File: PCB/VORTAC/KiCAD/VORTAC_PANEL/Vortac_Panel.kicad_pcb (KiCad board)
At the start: 4 copper layers, 80 x 80 mm, 103 parts, among them IC1 TMC2209-LA, J1 Conn_02x02_Odd_Even, J1 DEBUG, J14 918-418K2023S40001, J15 STEPPER, J2 Conn_02x03_Odd_Even, J3 Conn_01x07, J3 Conn_02x02_Odd_Even, SW1 Boot, SW2 Reset, U1 TLV73333PDBV, U2 STM32F103C8T6, U3 EE-SX4320, U5 AS5047D, U6 AP63205WU, U7 EE-SX3350, U8 TJA1044GTK/3Z, X1 Logo Gold, Y1 8MHz

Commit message: Panel Progress
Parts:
- removed the mouse-bite-2mm-slot at (98.8, 49.0)
- removed the mouse-bite-2mm-slot at (121.0, 73.0)
- added D1: SP0502BAHT, Package_TO_SOT_SMD:SOT-23, B.Cu at (91.5, 90.8)
- added D1: SP0502BAHT, Package_TO_SOT_SMD:SOT-23, B.Cu at (104.1, 105.5)
- added D1: SP0502BAHT, Package_TO_SOT_SMD:SOT-23, B.Cu at (91.6, 108.2)
- added D1: SP0502BAHT, Package_TO_SOT_SMD:SOT-23, B.Cu at (138.6, 108.2)
- added D2: SP0502BAHT, Package_TO_SOT_SMD:SOT-23, B.Cu at (81.8, 90.8)
- added D2: SP0502BAHT, Package_TO_SOT_SMD:SOT-23, B.Cu at (128.8, 108.2)
- added D2: SP0502BAHT, Package_TO_SOT_SMD:SOT-23, B.Cu at (81.8, 108.2)
- added D2: SP0502BAHT, Package_TO_SOT_SMD:SOT-23, B.Cu at (113.8, 105.6)
- added H1: MountingHole_Pad, Vortac:MountingHole_2.2mm_M2_Pad_Via_NTR, B.Cu at (77.6, 84.6)
- added H1: MountingHole_Pad, Vortac:MountingHole_2.2mm_M2_Pad_Via_NTR, B.Cu at (118.0, 111.7)
- added H1: MountingHole_Pad, Vortac:MountingHole_2.2mm_M2_Pad_Via_NTR, B.Cu at (77.6, 102.0)
- added H1: MountingHole_Pad, Vortac:MountingHole_2.2mm_M2_Pad_Via_NTR, B.Cu at (124.6, 102.0)
- added H2: MountingHole_Pad, Vortac:MountingHole_2.2mm_M2_Pad_Via_NTR, B.Cu at (143.0, 109.6)
- added H2: MountingHole_Pad, Vortac:MountingHole_2.2mm_M2_Pad_Via_NTR, B.Cu at (96.0, 109.6)
- added H2: MountingHole_Pad, Vortac:MountingHole_2.2mm_M2_Pad_Via_NTR, B.Cu at (99.7, 104.2)
- added H2: MountingHole_Pad, Vortac:MountingHole_2.2mm_M2_Pad_Via_NTR, B.Cu at (96.0, 92.2)
- added J1: Conn_01x07, Vortac:mill-max-0881-1-15-20-82-14-11-0_LandingPads_ContactPad_PTH_2x1.5x1, B.Cu at (127.6, 104.8)
- added J1: Conn_01x07, Vortac:mill-max-0881-1-15-20-82-14-11-0_LandingPads_ContactPad_PTH_2x1.5x1, B.Cu at (80.5, 87.4)
- added J1: Conn_01x07, Vortac:mill-max-0881-1-15-20-82-14-11-0_LandingPads_ContactPad_PTH_2x1.5x1, B.Cu at (115.1, 109.0)
- added J1: Conn_01x07, Vortac:mill-max-0881-1-15-20-82-14-11-0_LandingPads_ContactPad_PTH_2x1.5x1, B.Cu at (80.6, 104.8)
- added J2: Conn_01x02, Vortac:Toolplate_Solderpoint_01x02_Power, B.Cu at (123.9, 112.2)
- added J2: Conn_01x02, Vortac:Toolplate_Solderpoint_01x02_Power, B.Cu at (118.7, 101.5)
- added J2: Conn_01x02, Vortac:Toolplate_Solderpoint_01x02_Power, B.Cu at (76.9, 112.2)
- added J2: Conn_01x02, Vortac:Toolplate_Solderpoint_01x02_Power, B.Cu at (76.9, 94.8)
- added J3: Conn_01x05, Vortac:Toolplate_Solderpoint_01x05_Data, B.Cu at (83.8, 112.9)
- added J3: Conn_01x05, Vortac:Toolplate_Solderpoint_01x05_Data, B.Cu at (83.8, 95.5)
- added J3: Conn_01x05, Vortac:Toolplate_Solderpoint_01x05_Data, B.Cu at (130.8, 112.9)
- added J3: Conn_01x05, Vortac:Toolplate_Solderpoint_01x05_Data, B.Cu at (111.8, 100.8)
- added mouse-bite-2mm-slot: VAL**, Vortac:mouse-bite-2mm-slot, F.Cu at (130.4, 98.2)
- added mouse-bite-2mm-slot: VAL**, Vortac:mouse-bite-2mm-slot, F.Cu at (85.0, 98.2)
- added mouse-bite-2mm-slot: VAL**, Vortac:mouse-bite-2mm-slot, F.Cu at (130.9, 115.6)
- added mouse-bite-2mm-slot: VAL**, Vortac:mouse-bite-2mm-slot, F.Cu at (131.8, 92.0)
- added mouse-bite-2mm-slot: VAL**, Vortac:mouse-bite-2mm-slot, F.Cu at (110.1, 115.6)
- added mouse-bite-2mm-slot: VAL**, Vortac:mouse-bite-2mm-slot, F.Cu at (110.4, 84.4)
- added mouse-bite-2mm-slot: VAL**, Vortac:mouse-bite-2mm-slot, F.Cu at (121.0, 72.9)
- added mouse-bite-2mm-slot: VAL**, Vortac:mouse-bite-2mm-slot, F.Cu at (81.0, 115.6)
- added mouse-bite-2mm-slot: VAL**, Vortac:mouse-bite-2mm-slot, F.Cu at (145.9, 93.5)
- added mouse-bite-2mm-slot: VAL**, Vortac:mouse-bite-2mm-slot, F.Cu at (96.3, 49.0)
- added mouse-bite-2mm-slot: VAL**, Vortac:mouse-bite-2mm-slot, F.Cu at (85.8, 80.8)
- added mouse-bite-2mm-slot: VAL**, Vortac:mouse-bite-2mm-slot, F.Cu at (109.6, 98.2)
- added mouse-bite-2mm-slot: VAL**, Vortac:mouse-bite-2mm-slot, F.Cu at (90.0, 115.6)
- added mouse-bite-2mm-slot: VAL**, Vortac:mouse-bite-2mm-slot, F.Cu at (95.3, 84.8)
- moved ? 10.8 mm to (141.2, 119.6) (x2)
- moved ? 10.8 mm to (141.2, 45.0) (x2)
- moved REF** 9.83 mm to (146.2, 119.6)
- moved ? 9.81 mm to (146.2, 45.0)
- moved REF** 2.24 mm to (79.8, 119.6)
- moved ? 2.17 mm to (79.8, 45.0)
- moved ? 1.30 mm to (84.8, 119.6)
- moved REF** 1.30 mm to (84.8, 119.6)
- moved ? 1.17 mm to (84.8, 45.0) (x2)
- moved mouse-bite-2mm-slot 0.40 mm to (128.7, 49.0)
- moved mouse-bite-2mm-slot 0.30 mm to (144.4, 73.1)
- moved mouse-bite-2mm-slot 0.30 mm to (136.8, 73.1)
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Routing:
- net USB_90_D-: track 0.00 -> 52.0 mm
- net TOOL_ID: track 0.00 -> 46.7 mm
- net CAN_H: track 62.4 -> 107.8 mm
- net USB_90_D+: track 0.00 -> 39.2 mm
- net CAN_L: track 58.2 -> 96.2 mm
- added copper zone on F.Cu, net VDC
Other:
- board size 80 x 80 mm -> 76.4 x 80.6 mm
- board text added: "25.05.25"
- board text added: "VORTAC REV01"
- board text added: "by Joel & Henny"

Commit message: updated Outlines
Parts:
- removed the D1 at (91.5, 90.8)
- removed the D1 at (104.1, 105.5)
- removed the D1 at (91.6, 108.2)
- removed the D1 at (138.6, 108.2)
- removed the D2 at (81.8, 90.8)
- removed the D2 at (128.8, 108.2)
- removed the D2 at (81.8, 108.2)
- removed the D2 at (113.8, 105.6)
- removed the H1 at (77.6, 84.6)
- removed the H1 at (118.0, 111.7)
- removed the H1 at (77.6, 102.0)
- removed the H1 at (124.6, 102.0)
- removed the H2 at (143.0, 109.6)
- removed the H2 at (96.0, 109.6)
- removed the H2 at (99.7, 104.2)
- removed the H2 at (96.0, 92.2)
- removed the J1 at (127.6, 104.8)
- removed the J1 at (80.5, 87.4)
- removed the J1 at (115.1, 109.0)
- removed the J1 at (80.6, 104.8)
- removed the J2 at (123.9, 112.2)
- removed the J2 at (118.7, 101.5)
- removed the J2 at (76.9, 112.2)
- removed the J2 at (76.9, 94.8)
- removed the J3 at (83.8, 112.9)
- removed the J3 at (83.8, 95.5)
- removed the J3 at (130.8, 112.9)
- removed the J3 at (111.8, 100.8)
- removed the mouse-bite-2mm-slot at (130.4, 98.2)
- removed the mouse-bite-2mm-slot at (85.0, 98.2)
- removed the mouse-bite-2mm-slot at (130.9, 115.6)
- removed the mouse-bite-2mm-slot at (110.1, 115.6)
- removed the mouse-bite-2mm-slot at (110.4, 84.4)
- removed the mouse-bite-2mm-slot at (81.0, 115.6)
- removed the mouse-bite-2mm-slot at (85.8, 80.8)
- removed the mouse-bite-2mm-slot at (109.6, 98.2)
- removed the mouse-bite-2mm-slot at (90.0, 115.6)
- removed the mouse-bite-2mm-slot at (95.3, 84.8)
- added D1: UDD32C24L01, Diode_SMD:D_SOD-323, F.Cu at (135.3, 103.5)
- added D1: UDD32C24L01, Diode_SMD:D_SOD-323, F.Cu at (86.9, 103.5)
- added D1: UDD32C24L01, Diode_SMD:D_SOD-323, F.Cu at (102.4, 110.3)
- added D1: UDD32C24L01, Diode_SMD:D_SOD-323, F.Cu at (86.9, 86.1)
- added D2: UDD32C24L01, Diode_SMD:D_SOD-323, F.Cu at (137.2, 103.5)
- added D2: UDD32C24L01, Diode_SMD:D_SOD-323, F.Cu at (100.5, 110.3)
- added D2: UDD32C24L01, Diode_SMD:D_SOD-323, F.Cu at (88.8, 103.5)
- added D2: UDD32C24L01, Diode_SMD:D_SOD-323, F.Cu at (88.8, 86.1)
- added D3: SD05, Diode_SMD:D_SOD-323, F.Cu at (106.8, 110.3)
- added D3: SD05, Diode_SMD:D_SOD-323, F.Cu at (82.5, 103.5)
- added D3: SD05, Diode_SMD:D_SOD-323, F.Cu at (131.0, 103.5)
- added D3: SD05, Diode_SMD:D_SOD-323, F.Cu at (82.5, 86.1)
- added D4: SD05, Diode_SMD:D_SOD-323, F.Cu at (104.9, 110.3)
- added D4: SD05, Diode_SMD:D_SOD-323, F.Cu at (84.4, 103.5)
- added D4: SD05, Diode_SMD:D_SOD-323, F.Cu at (132.9, 103.5)
- added D4: SD05, Diode_SMD:D_SOD-323, F.Cu at (84.4, 86.1)
- added D9: PTVS26VS1UR,115-ES, Diode_SMD:D_SOD-123F, F.Cu at (78.5, 87.2)
- added D9: PTVS26VS1UR,115-ES, Diode_SMD:D_SOD-123F, F.Cu at (110.8, 109.1)
- added D9: PTVS26VS1UR,115-ES, Diode_SMD:D_SOD-123F, F.Cu at (126.9, 104.6)
- added D9: PTVS26VS1UR,115-ES, Diode_SMD:D_SOD-123F, F.Cu at (78.5, 104.6)
- added H1: MountingHole_Pad, Vortac:MountingHole_2.2mm_M2_Pad_Via_NTR, F.Cu at (74.0, 111.7)
- added H1: MountingHole_Pad, Vortac:MountingHole_2.2mm_M2_Pad_Via_NTR, F.Cu at (115.3, 102.0)
- added H1: MountingHole_Pad, Vortac:MountingHole_2.2mm_M2_Pad_Via_NTR, F.Cu at (74.0, 94.3)
- added H1: MountingHole_Pad, Vortac:MountingHole_2.2mm_M2_Pad_Via_NTR, F.Cu at (122.4, 111.7)
- added H2: MountingHole_Pad, Vortac:MountingHole_2.2mm_M2_Pad_Via_NTR, F.Cu at (140.8, 104.2)
- added H2: MountingHole_Pad, Vortac:MountingHole_2.2mm_M2_Pad_Via_NTR, F.Cu at (92.3, 86.8)
- added H2: MountingHole_Pad, Vortac:MountingHole_2.2mm_M2_Pad_Via_NTR, F.Cu at (97.0, 109.6)
- added H2: MountingHole_Pad, Vortac:MountingHole_2.2mm_M2_Pad_Via_NTR, F.Cu at (92.3, 104.2)
- added J1: Conn_01x07, Vortac:mill-max-0881-1-15-20-82-14-11-0_LandingPads_ContactPad_PTH_2x1.5x1, F.Cu at (76.9, 109.0)
- added J1: Conn_01x07, Vortac:mill-max-0881-1-15-20-82-14-11-0_LandingPads_ContactPad_PTH_2x1.5x1, F.Cu at (76.9, 91.6)
- added J1: Conn_01x07, Vortac:mill-max-0881-1-15-20-82-14-11-0_LandingPads_ContactPad_PTH_2x1.5x1, F.Cu at (112.4, 104.8)
- added J1: Conn_01x07, Vortac:mill-max-0881-1-15-20-82-14-11-0_LandingPads_ContactPad_PTH_2x1.5x1, F.Cu at (125.4, 109.0)
- added J2: Conn_01x02, Vortac:Toolplate_Solderpoint_01x02_Power, F.Cu at (73.3, 84.1)
- added J2: Conn_01x02, Vortac:Toolplate_Solderpoint_01x02_Power, F.Cu at (121.7, 101.5)
- added J2: Conn_01x02, Vortac:Toolplate_Solderpoint_01x02_Power, F.Cu at (73.3, 101.5)
- added J2: Conn_01x02, Vortac:Toolplate_Solderpoint_01x02_Power, F.Cu at (116.0, 112.2)
- added J3: Conn_01x05, Vortac:Toolplate_Solderpoint_01x05_Data, F.Cu at (80.2, 100.8)
- added J3: Conn_01x05, Vortac:Toolplate_Solderpoint_01x05_Data, F.Cu at (128.6, 100.8)
- added J3: Conn_01x05, Vortac:Toolplate_Solderpoint_01x05_Data, F.Cu at (109.2, 112.9)
- added J3: Conn_01x05, Vortac:Toolplate_Solderpoint_01x05_Data, F.Cu at (80.2, 83.4)
- added mouse-bite-2mm-slot: VAL**, Vortac:mouse-bite-2mm-slot, F.Cu at (105.4, 98.2)
- added mouse-bite-2mm-slot: VAL**, Vortac:mouse-bite-2mm-slot, F.Cu at (81.4, 115.6)
- added mouse-bite-2mm-slot: VAL**, Vortac:mouse-bite-2mm-slot, F.Cu at (128.2, 98.2)
- added mouse-bite-2mm-slot: VAL**, Vortac:mouse-bite-2mm-slot, F.Cu at (74.9, 80.8)
- added mouse-bite-2mm-slot: VAL**, Vortac:mouse-bite-2mm-slot, F.Cu at (108.1, 84.4)
- added mouse-bite-2mm-slot: VAL**, Vortac:mouse-bite-2mm-slot, F.Cu at (131.0, 115.6)
- added mouse-bite-2mm-slot: VAL**, Vortac:mouse-bite-2mm-slot, F.Cu at (75.0, 49.0)
- added mouse-bite-2mm-slot: VAL**, Vortac:mouse-bite-2mm-slot, F.Cu at (91.7, 94.2)
- added mouse-bite-2mm-slot: VAL**, Vortac:mouse-bite-2mm-slot, F.Cu at (106.7, 115.6)
- added mouse-bite-2mm-slot: VAL**, Vortac:mouse-bite-2mm-slot, F.Cu at (81.4, 98.2)
- added mouse-bite-2mm-slot: VAL**, Vortac:mouse-bite-2mm-slot, F.Cu at (86.7, 80.8)
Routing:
- net USB_90_D+: track 39.2 -> 59.0 mm
- net VDC: track 45.6 -> 57.8 mm
- net CAN_L: track 96.2 -> 104.0 mm
- net USB_90_D-: track 52.0 -> 59.6 mm
- net TOOL_ID: track 46.7 -> 48.4 mm
- net CAN_H: track 107.8 -> 108.9 mm
- net GND: vias 73 -> 157
- removed copper zone on F.Cu, net VDC
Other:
- board size 76.4 x 80.6 mm -> 80 x 80.6 mm
- board text added: "CH"
- board text added: "CL"
- board text added: "DM"
- board text added: "DP"
- board text added: "ID"
- board text added: "V+"

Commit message: Logo Vector Panel Updates Logo Footprint Test
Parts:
- added REF**: Panel_Logo, Vortac:Panel_Logo, F.Cu at (108.4, 91.5)
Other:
- board text removed: "by Joel & Henny"

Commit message: idk
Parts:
- removed the REF** at (108.4, 91.5)
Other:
- board text added: "BEWARE: pcb may spontaneously teleport tools"
- board text added: "JLCJLCJLCJLC"
- board text added: "Made by Aliens with Love ❤"
- board text added: "Prt_Rik"
- board text added: "Quantum Binary 3D Printing ♥"
- board text added: "Warning: removing a tool induces quantum decoherence"
- board text added: "Warning: superposition of tools may induce loss of coherence"
- board text added: "alien 3d printing technology"
- board text added: "calibrated under the Born-Oppenheimer approximation"
- board text added: "entangle free quantum 3d printing"
- board text added: "entanglement free quantum 3d printing"
- board text added: "high-frequency omnidirectional print tool navigation"
- board text added: "this isn't a bug, it's an interdimensional feature"
- board text added: "tolerances may violate Heisenberg's uncertainty principle"
- board text added: "tool superposition"
- board text added: "tool superposition requires TOOL ID to be Qubit"
- board text added: "very high frequency omnidirectional remote tool assembly communication"
- board text added: "your stealthburner's personal VORTAC beacon"
- board text added: "{dblquote}VORTAC{dblquote} is an aviation navigation system combining VOR (Very High Frequency Omnidirectional Radio Range) and TACAN (Tactical Air Navigation). VORTAC is used by both civilian and military aircraft for navigation and landing guidance."

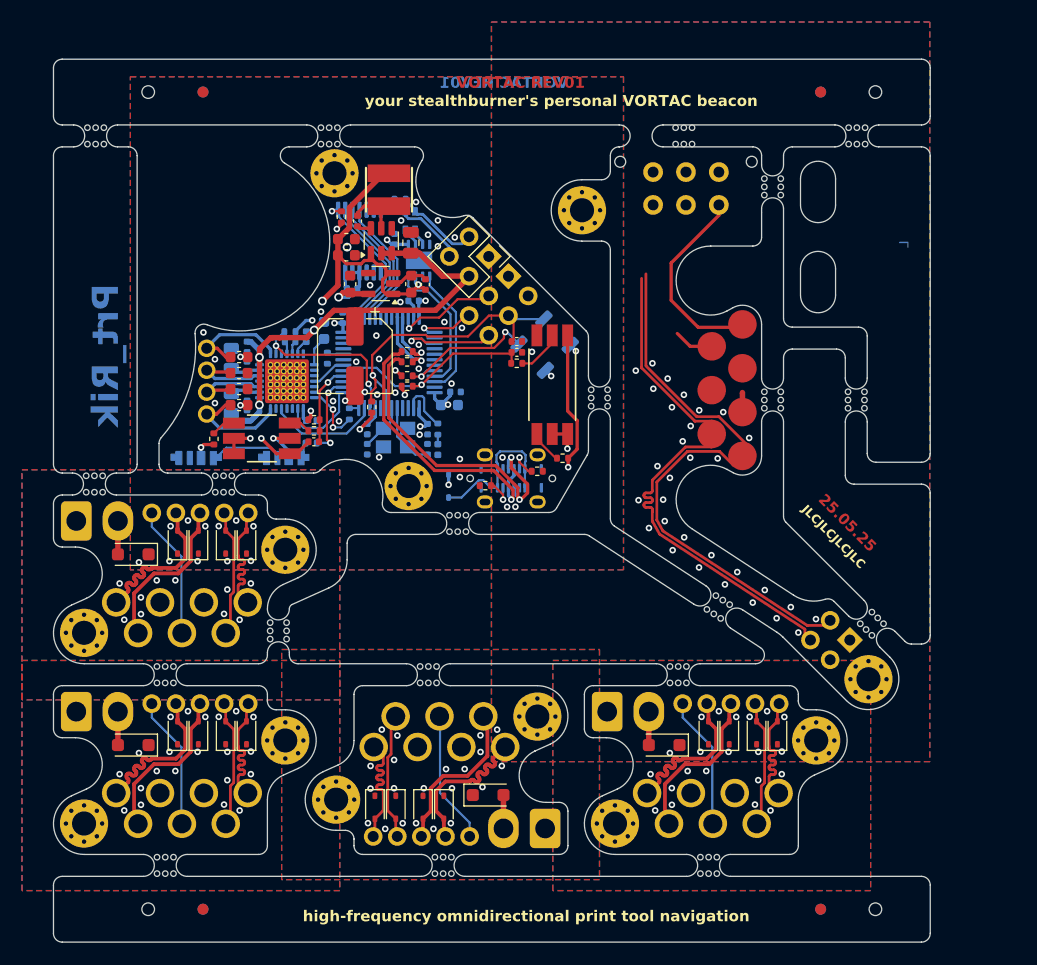
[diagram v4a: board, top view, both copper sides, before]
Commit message: updated Panel
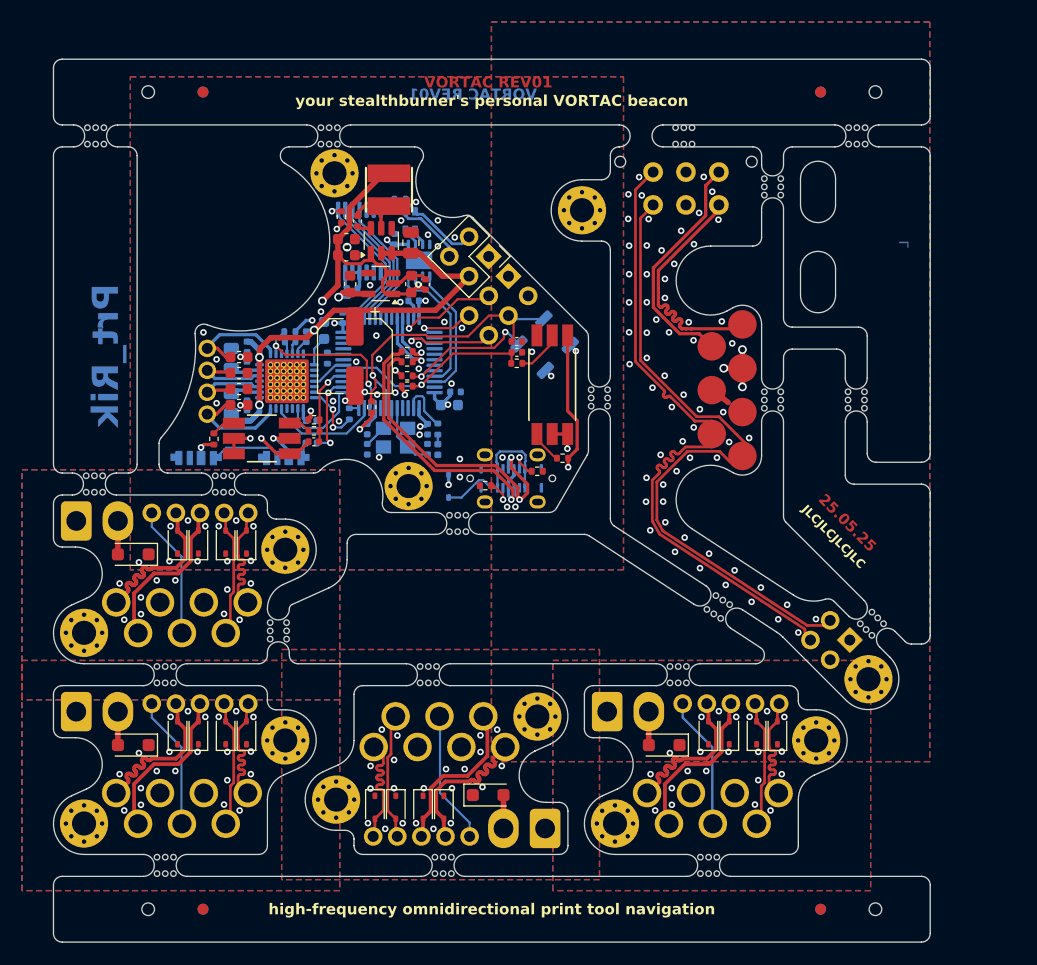
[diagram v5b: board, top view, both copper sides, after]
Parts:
- removed X1: Logo Gold, Vortac:VORTAC_Logo_Gold
- R30, R34: value 0.22R 1% -> 0.68R 1%
- U7: value EE-SX3350 -> EE-SX4350
- moved NT1 1.70 mm to (132.4, 73.0), turned to -38 degrees
- moved J15 0.05 mm to (85.2, 74.4)
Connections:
- J2 pad 1: CAN_L -> CAN_H
- J2 pad 2: GND -> VDC
- J2 pad 4: CAN_H -> CAN_L
- J2 pad 5: VDC -> GND
- J3 pad 3: GND -> VDC
- J3 pad 4: VDC -> TOOL_ID
- J3 pad 5: TOOL_ID -> GND
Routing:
- net USB_D-: track 32.8 -> 50.7 mm
- net CAN_L: track 104.0 -> 115.1 mm
- net CAN_H: track 108.9 -> 115.8 mm
- net USB_D+: track 42.9 -> 48.3 mm
- net VDC: track 57.8 -> 62.9 mm, vias 3 -> 6
- net GND: vias 157 -> 189
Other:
- board text added: "BOOT"
